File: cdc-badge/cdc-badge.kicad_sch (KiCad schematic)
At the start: 145 parts, among them J1 USB_C, J2 JST S2B-PH-SM4-TB, J3 Conn_02x20_Odd_Even, J4 Conn_Grove, J5 Conn_02x03_Odd_Even, J6 Conn_01x06, J7 Conn_01x24, Q1 Si1308EDL, Q2 SS8050, SW0 0, SW1 1, SW10 YES, SW11 NO, SW12 power on/reset, SW13 reset, SW14 flash/power off, SW15 MST-22D18G2 3J, SW16 MST-22D18G2 3J, SW2 2, SW3 3, SW4 4, SW5 5, SW6 6, SW7 7, SW8 8, SW9 9, U1 ESP32-S3-WROOM-1-N16R8, U2 TCA9535PWR, U3 TROPIC01, U4 TPS613222ADBV, U6 BQ25895RTW, U7 USBLC6-2SC6, U8 TLV62569DBV

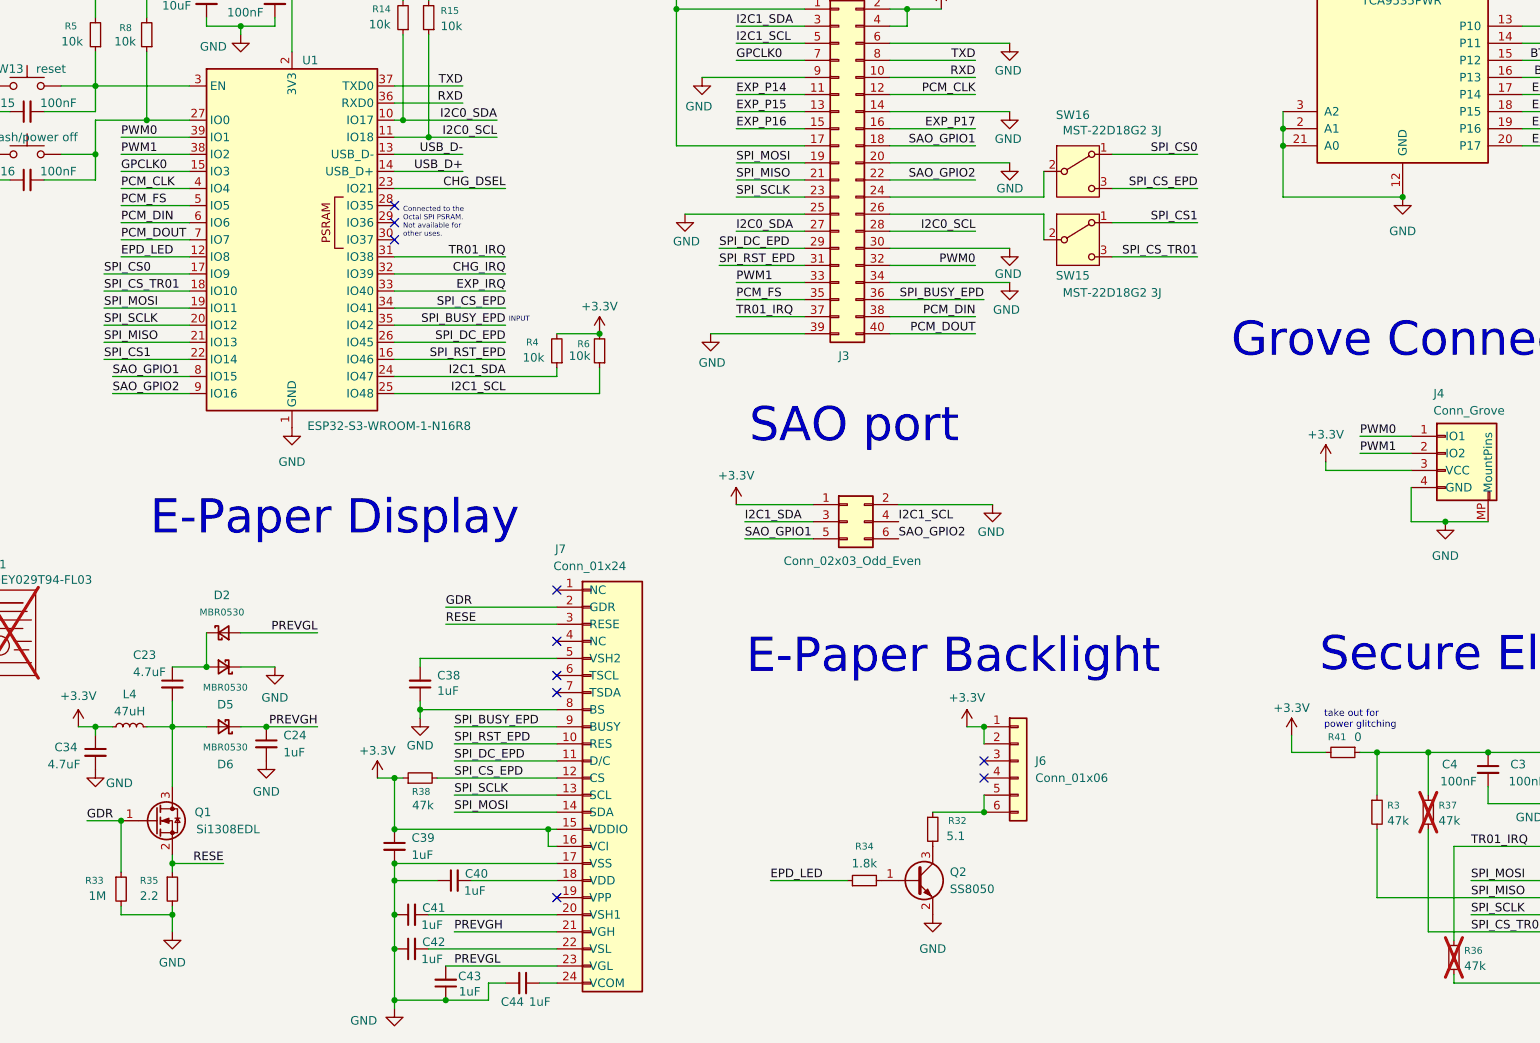
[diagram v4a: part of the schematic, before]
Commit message: schematic: fix frontlight connector orientation
The Jushuo connector we are using has its pins numbered in the reverse
order of the frontlight connector shown on the GDEY029T94-FL03
datasheet.
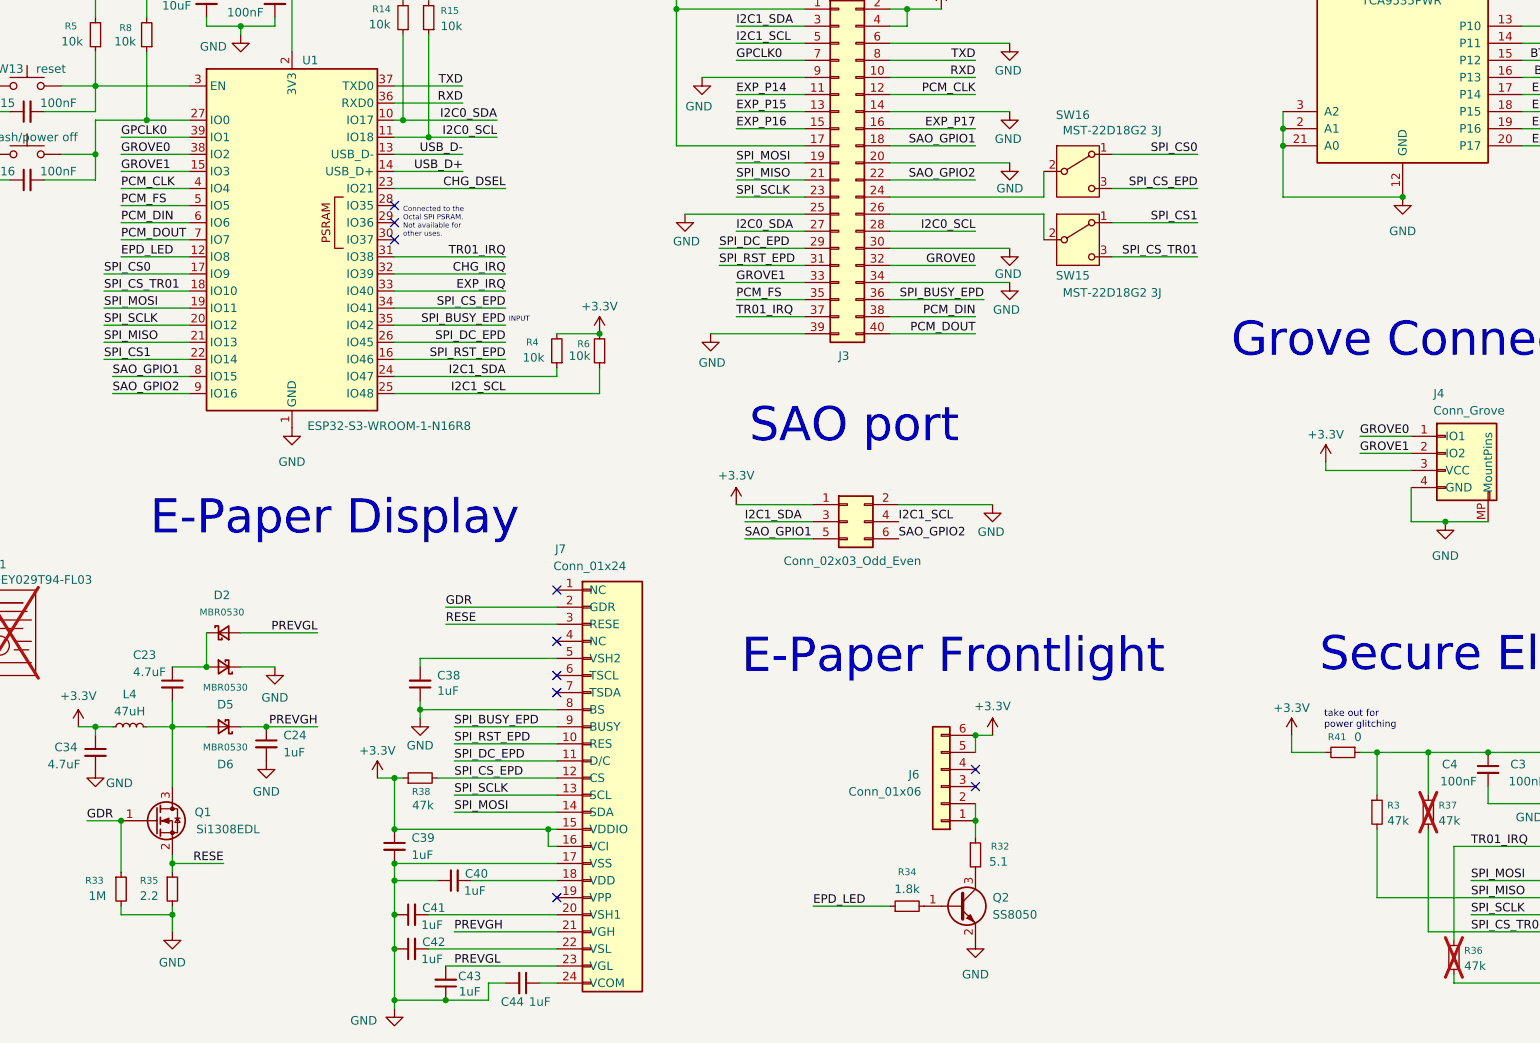
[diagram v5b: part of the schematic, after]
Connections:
- net +3.3V: now also J6.5 (Pin_5), J6.6 (Pin_6); no longer J6.1 (Pin_1), J6.2 (Pin_2)
- net GPCLK0: now also U1.39 (IO1); no longer U1.15 (IO3)
- net PWM0 renamed GROVE0
- net GROVE0: now also U1.38 (IO2); no longer U1.39 (IO1)
- net PWM1 renamed GROVE1
- net GROVE1: now also U1.15 (IO3); no longer U1.38 (IO2)
- new net: J6.1 (Pin_1), J6.2 (Pin_2), R32.1
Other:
- note added: "E-Paper Frontlight"
- note removed: "E-Paper Backlight"
- moved on the sheet: J6, Q2, R32, R34

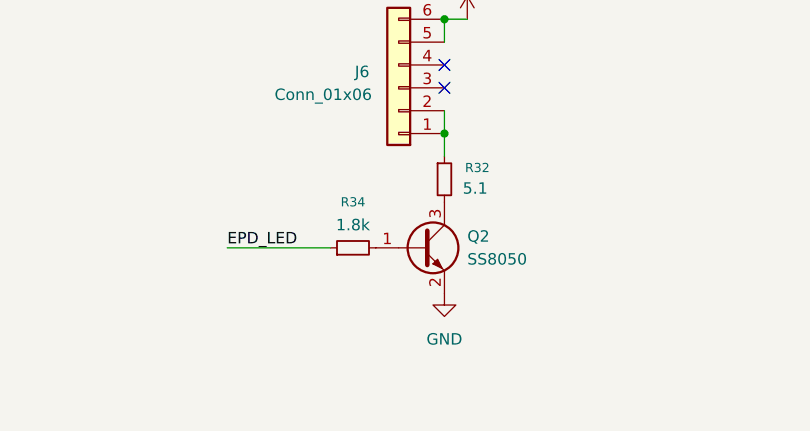
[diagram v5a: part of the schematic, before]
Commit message: schematic: ceetee reviews, e-paper frontlight
Replace BJT for MOSFET. One less part in BOM.
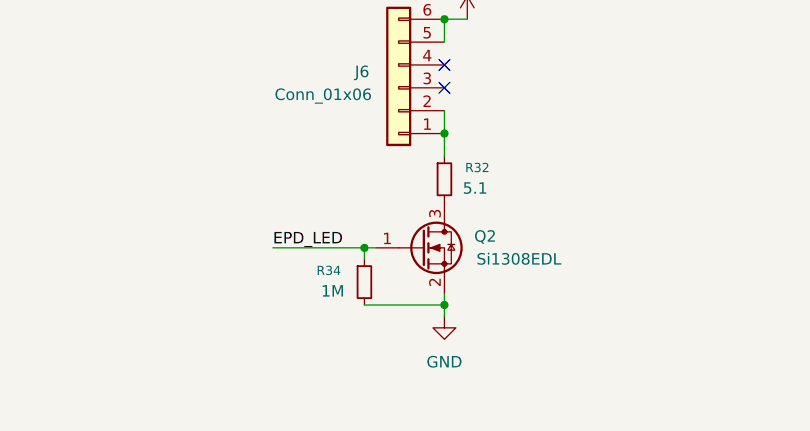
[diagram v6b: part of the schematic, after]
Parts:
- removed Q2: SS8050, Package_TO_SOT_SMD:SOT-23, symbol Transistor_BJT:SS8050
- added Q2: Si1308EDL, Package_TO_SOT_SMD:SOT-323_SC-70, symbol Transistor_FET:Si1308EDL
- R34: value 1.8k -> 1M; JLCPCB PN C4177 -> C22935; MPN (none) -> 0603WAF1004T5E
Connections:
- net EPD_LED: now also Q2.1 (G)
- net GND: now also R34.2, Q2.2 (S)
- net at R32.2: now also Q2.3 (D)

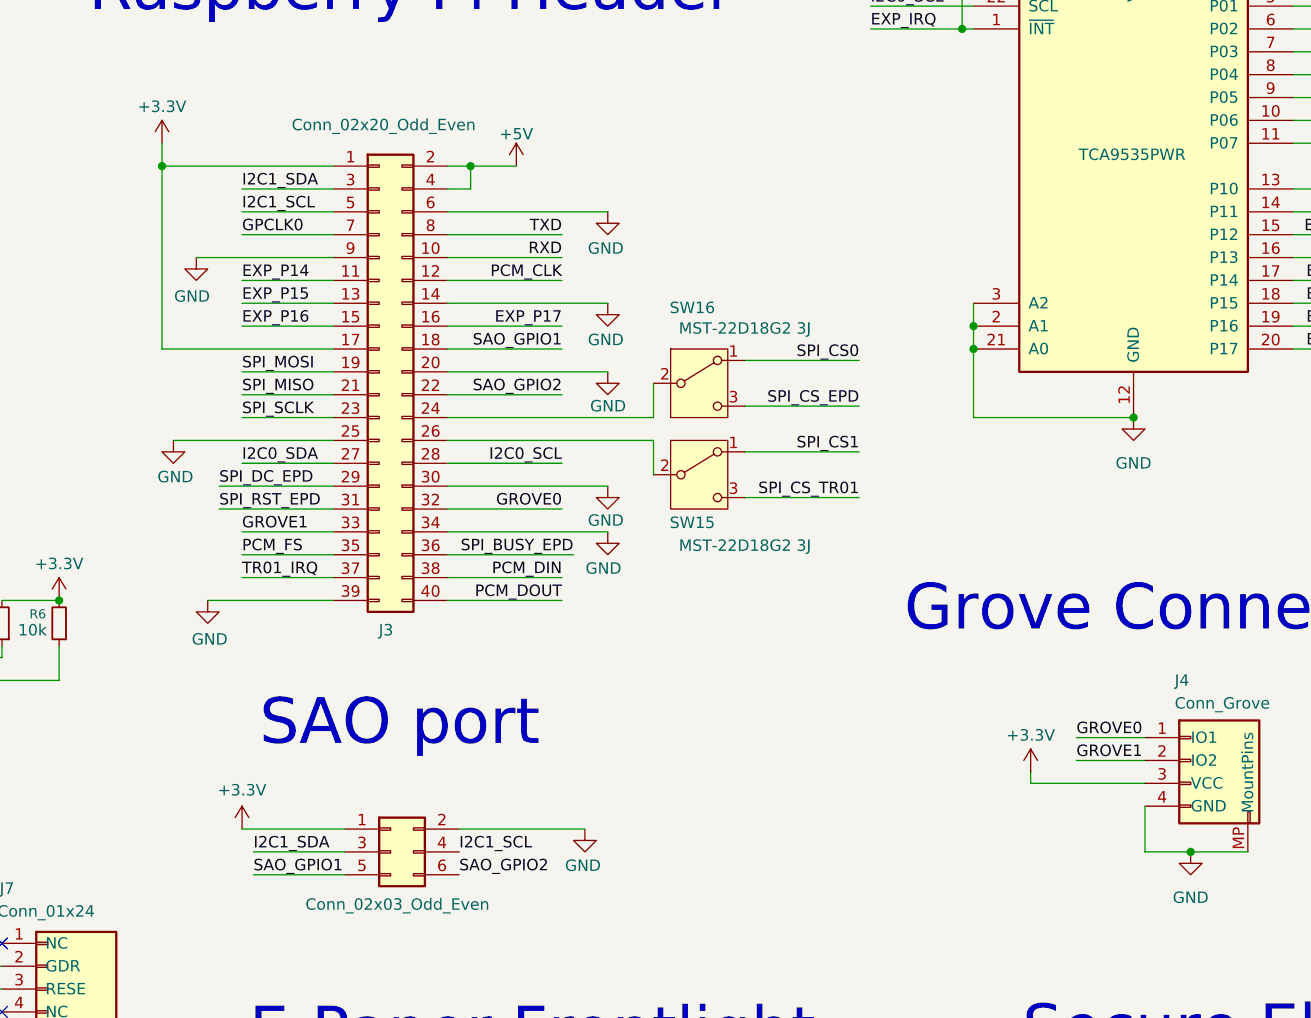
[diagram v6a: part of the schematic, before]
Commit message: schematic: ceetee reviews, add power output decoupling capacitors
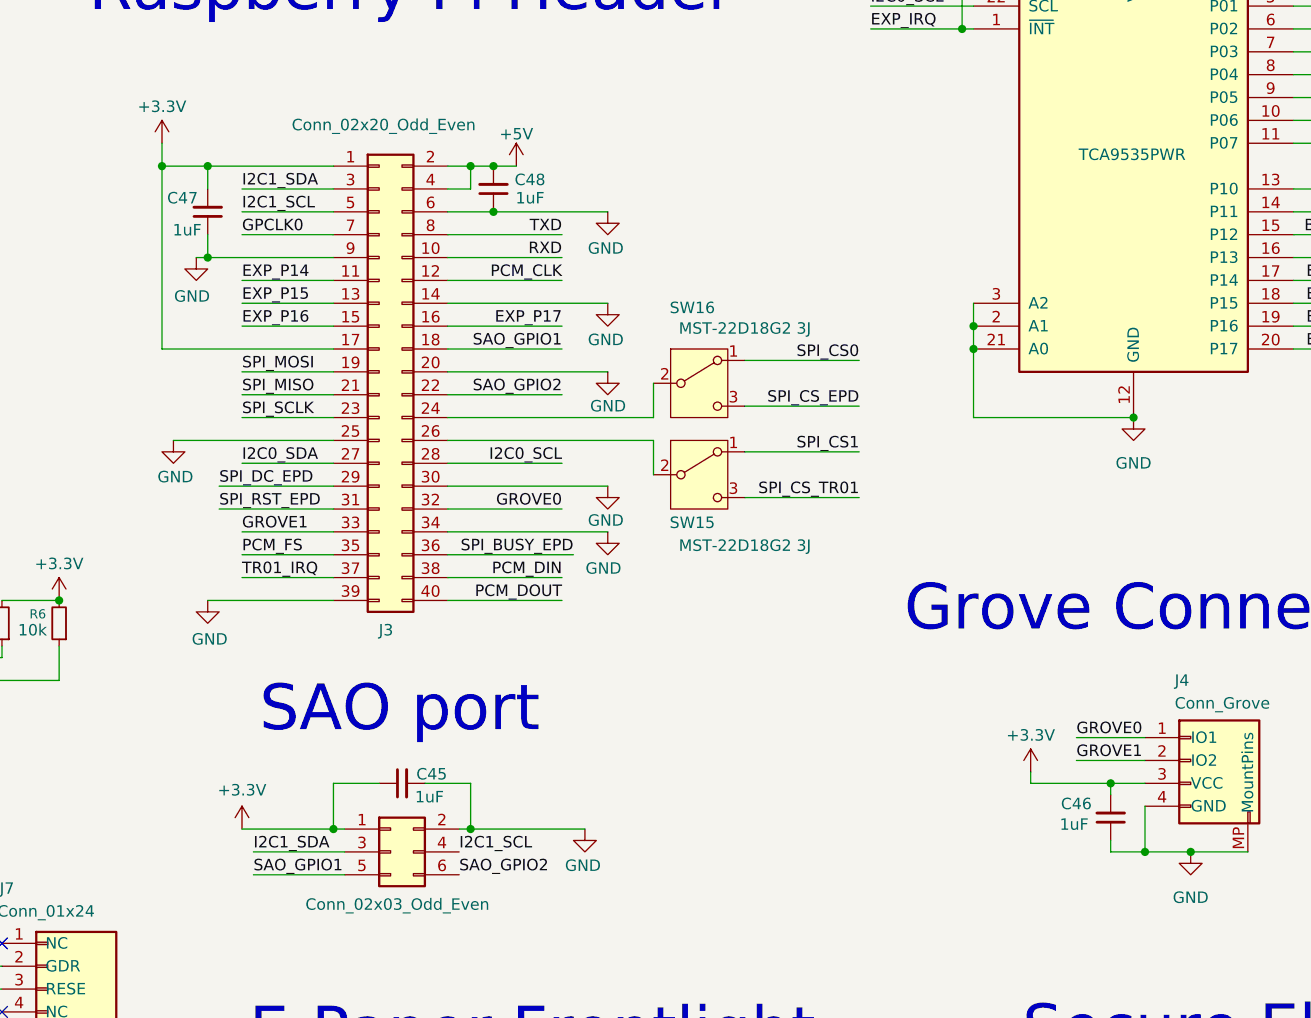
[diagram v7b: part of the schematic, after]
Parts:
- added C45, C46, C47, C48: 1uF, Capacitor_SMD:C_0603_1608Metric, symbol Device:C_Small
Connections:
- net +3.3V: now also C45.1, C46.2, C47.2
- net +5V: now also C48.2
- net GND: now also C45.2, C46.1, C47.1, C48.1

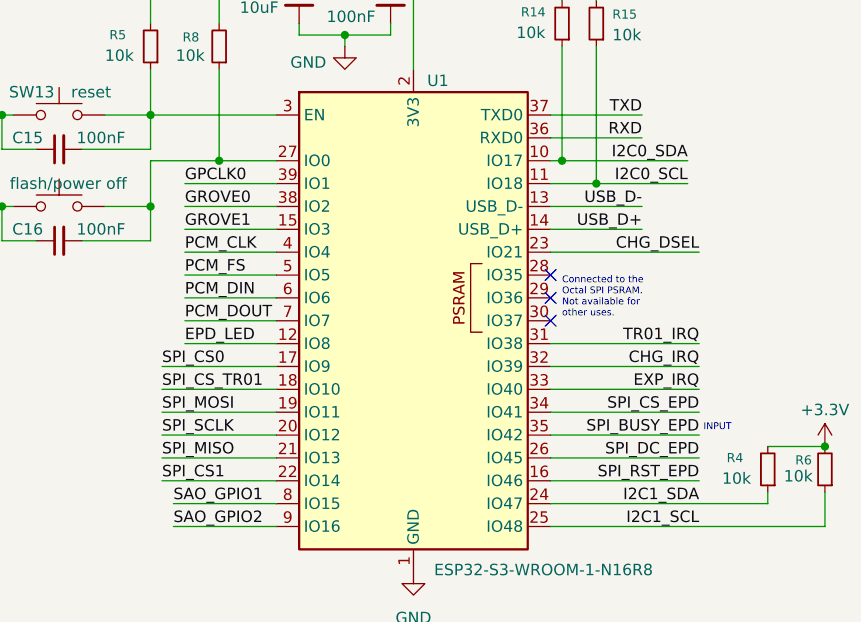
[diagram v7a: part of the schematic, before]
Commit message: schematic: ceetee reviews, fix ESP32 pin assignment
Move GPCLK to a pin with CLK_OUT support.
Swap SPI MOSI and MISO.
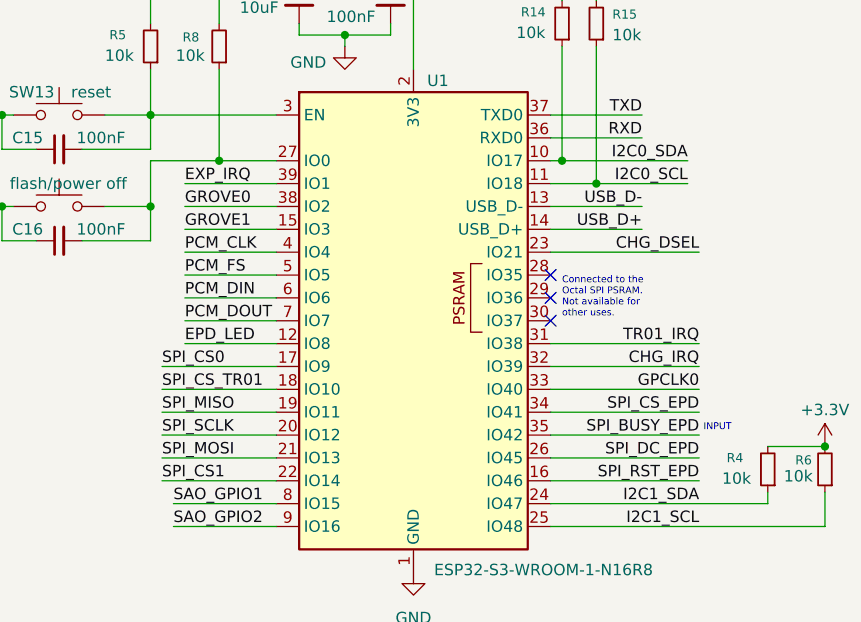
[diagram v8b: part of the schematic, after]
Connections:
- net EXP_IRQ: now also U1.39 (IO1); no longer U1.33 (IO40)
- net GPCLK0: now also U1.33 (IO40); no longer U1.39 (IO1)
- net SPI_MISO: now also U1.19 (IO11); no longer U1.21 (IO13)
- net SPI_MOSI: now also U1.21 (IO13); no longer U1.19 (IO11)
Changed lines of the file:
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@@
+		)
+	)
+	(label "GPCLK0"
+		(at 105.41 173.99 180)
+		(effects
+			(font
+				(size 1.27 1.27)
+			)
+			(justify right bottom)
 		)
 	)
@@
 		)
 	)
+	(label "EXP_IRQ"
+		(at 48.26 151.13 0)
+		(effects
+			(font
+				(size 1.27 1.27)
+			)
+			(justify left bottom)
+		)
+	)
 	(label "USB_D-"
 		(at 55.88 82.55 0)
@@
 		)
 	)
-	(label "SPI_MOSI"
+	(label "SPI_MISO"
 		(at 45.72 176.53 0)
 		(effects
@@
 			)
 			(justify left bottom)
-		)
-	)
-	(label "EXP_IRQ"
-		(at 105.41 173.99 180)
-		(effects
-			(font
-				(size 1.27 1.27)
-			)
-			(justify right bottom)
 		)
 	)
@@
 		)
 	)
-	(label "SPI_MISO"
+	(label "SPI_MOSI"
 		(at 45.72 181.61 0)
 		(effects
@@
 		)
 	)
-	(label "GPCLK0"
-		(at 48.26 151.13 0)
-		(effects
-			(font
-				(size 1.27 1.27)
-			)
-			(justify left bottom)
-		)
-	)
